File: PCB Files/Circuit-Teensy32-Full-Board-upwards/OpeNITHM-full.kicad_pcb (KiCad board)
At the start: 2 copper layers, 480 x 151 mm, 143 parts, among them J1 USB_C_Receptacle, J2 Conn_01x09, J3 Conn_01x09, J4 Conn_02x05_Odd_Even, J5 Conn_01x04, J6 Conn_01x04, J7 Barrel_Jack, J8 Conn_01x02, U1 Teensy-LC, U2 74HC4051D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

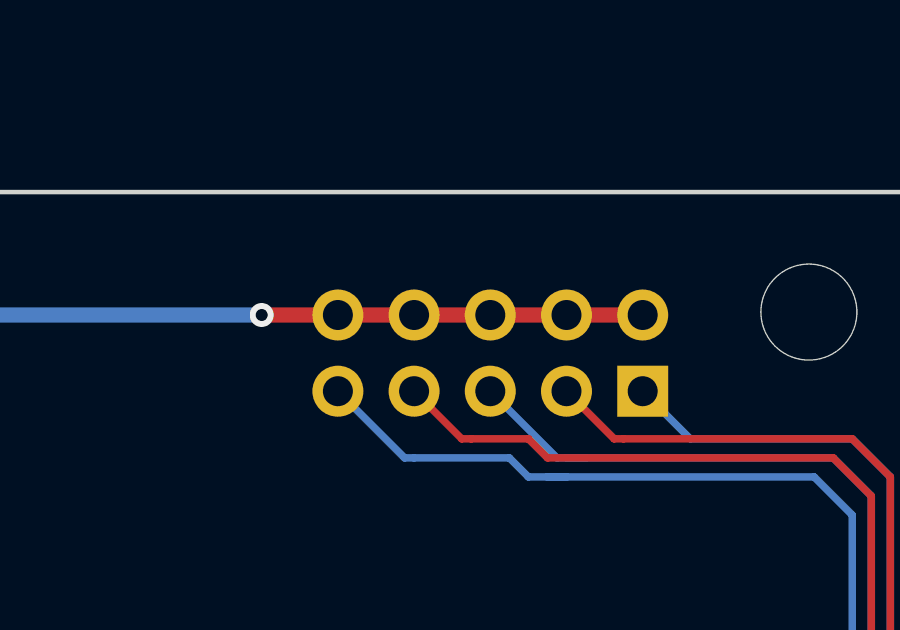
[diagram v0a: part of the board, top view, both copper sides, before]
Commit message: Minor trace edit. Has no impact on board function
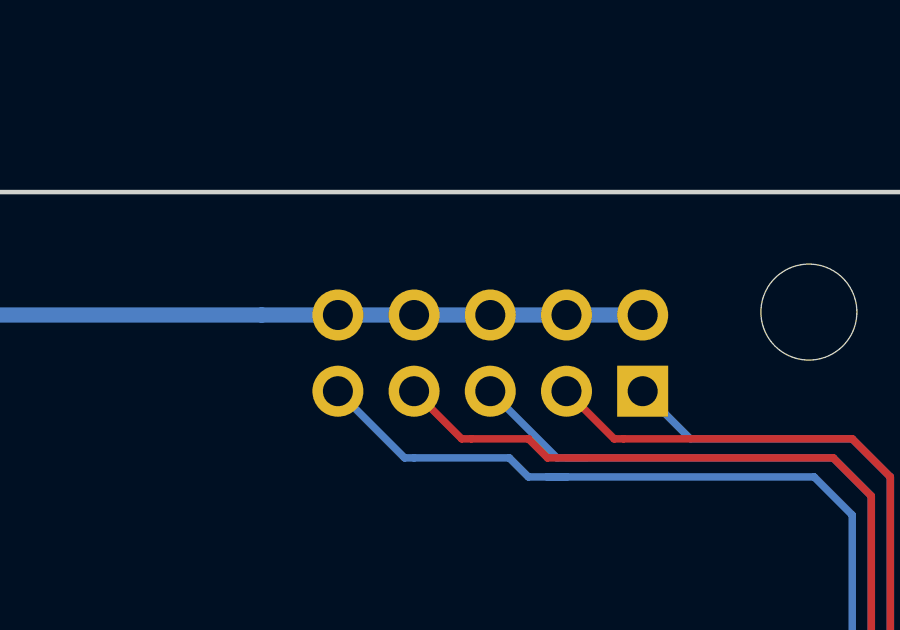
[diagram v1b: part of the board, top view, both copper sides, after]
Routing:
- net GND: vias 44 -> 43
